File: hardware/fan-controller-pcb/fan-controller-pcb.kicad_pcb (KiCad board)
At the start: 2 copper layers, 91 x 121.5 mm, 42 parts, among them J1 Screw_Terminal_01x04, J2 nc3fdm3-v, J3 nc3mdm3-v, SW1 SW_SPDT, SW2 SW_DIP_x10, U1 MC7812BDTG, U2 MC7805CDTG, U3 MCP4922, U4 TLC272, U5 MAX485E

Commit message: update PCB: edge cuts, routing, symbol_lib, footprint_lib, art & data sheets
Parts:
- added kibuzzard-63FA74A1: G***, kibuzzard-63FA74A1, F.Cu at (90.3, 40.0)
- added kibuzzard-63FA74BB: G***, kibuzzard-63FA74BB, F.Cu at (85.3, 40.0)
- added kibuzzard-63FA74F3: G***, kibuzzard-63FA74F3, F.Cu at (75.3, 40.0)
- added kibuzzard-63FA7528: G***, kibuzzard-63FA7528, F.Cu at (80.3, 40.0)
- added kibuzzard-640DCC4D: G***, kibuzzard-640DCC4D, F.Cu at (156.6, 39.0)
- added kibuzzard-640DCC52: G***, kibuzzard-640DCC52, F.Cu at (155.0, 73.3)
- added kibuzzard-640DCC68: G***, kibuzzard-640DCC68, F.Cu at (111.3, 127.3)
- added kibuzzard-640DCC6D: G***, kibuzzard-640DCC6D, F.Cu at (149.2, 126.5)
- added kibuzzard-640DCC72: G***, kibuzzard-640DCC72, F.Cu at (151.2, 91.9)
- added kibuzzard-640DCC79: G***, kibuzzard-640DCC79, F.Cu at (77.0, 127.3)
- added kibuzzard-640DCC82: G***, kibuzzard-640DCC82, F.Cu at (112.9, 65.4)
- added kibuzzard-640DCCF2: G***, kibuzzard-640DCCF2, F.Cu at (249.8, 90.2)
- moved C5 214.0 mm to (138.2, 106.8), turned to 0 degrees
- moved U4 213.7 mm to (140.0, 102.8), turned to 180 degrees
- moved U3 197.3 mm to (140.0, 93.0)
- moved R15 194.7 mm to (152.4, 103.0), turned to 180 degrees
- moved R17 194.1 mm to (152.4, 105.0), turned to 0 degrees
- moved C6 189.1 mm to (146.2, 93.3), turned to 90 degrees
- moved SW2 69.1 mm to (156.0, 53.0)
- moved SW1 66.0 mm to (145.0, 119.0)
- moved C4 55.3 mm to (126.5, 57.5), turned to 90 degrees
- moved C2 54.9 mm to (126.5, 40.6), turned to 90 degrees
- moved U2 52.1 mm to (120.0, 57.0), turned to -90 degrees
- moved U1 51.4 mm to (120.0, 40.0), turned to -90 degrees
- moved C3 48.5 mm to (113.5, 57.5), turned to 90 degrees
- moved C1 46.9 mm to (113.5, 40.6), turned to 90 degrees
- moved R16 41.9 mm to (120.0, 68.0)
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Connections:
- A1 pad 19: DIP_8 -> DIP_10
- A1 pad 21: DIP_10 -> DIP_8
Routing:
- net +5V: track 0.00 -> 140.1 mm, vias 0 -> 4
- net Net-(J1-Pad3): track 0.00 -> 130.1 mm
- net +12V: track 0.00 -> 123.8 mm, vias 0 -> 1
- net +24V: track 0.00 -> 78.9 mm
- net DIP_8: track 0.00 -> 64.7 mm
- net DIP_10: track 0.00 -> 64.2 mm
- net DIP_9: track 0.00 -> 64.2 mm
- net DMX_D+: track 0.00 -> 64.1 mm
- net DMX_D-: track 0.00 -> 61.9 mm
- net Net-(D1-Pad2): track 0.00 -> 49.4 mm, vias 0 -> 1
- net 1.6V-10V_2: track 0.00 -> 47.2 mm
- net DIP_3: track 0.00 -> 44.1 mm
- net DIP_2: track 0.00 -> 43.9 mm
- net DIP_1: track 0.00 -> 43.7 mm
- net DIP_4: track 0.00 -> 43.2 mm
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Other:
- board size 91 x 121.5 mm -> 100 x 130 mm
- board text added: "DMX0"
- board text added: "DMX1"
- board text added: "DMX2"
- board text added: "DMX3"
- board text added: "DMX4"
- board text added: "DMX5"
- board text added: "DMX6"
- board text added: "DMX7"
- board text added: "DMX8"
- board text added: "FUNC"
- board text added: "GND"
- board text added: "LED+"
- board text added: "github.com/LennardBoediger/dmx-fan-controller"

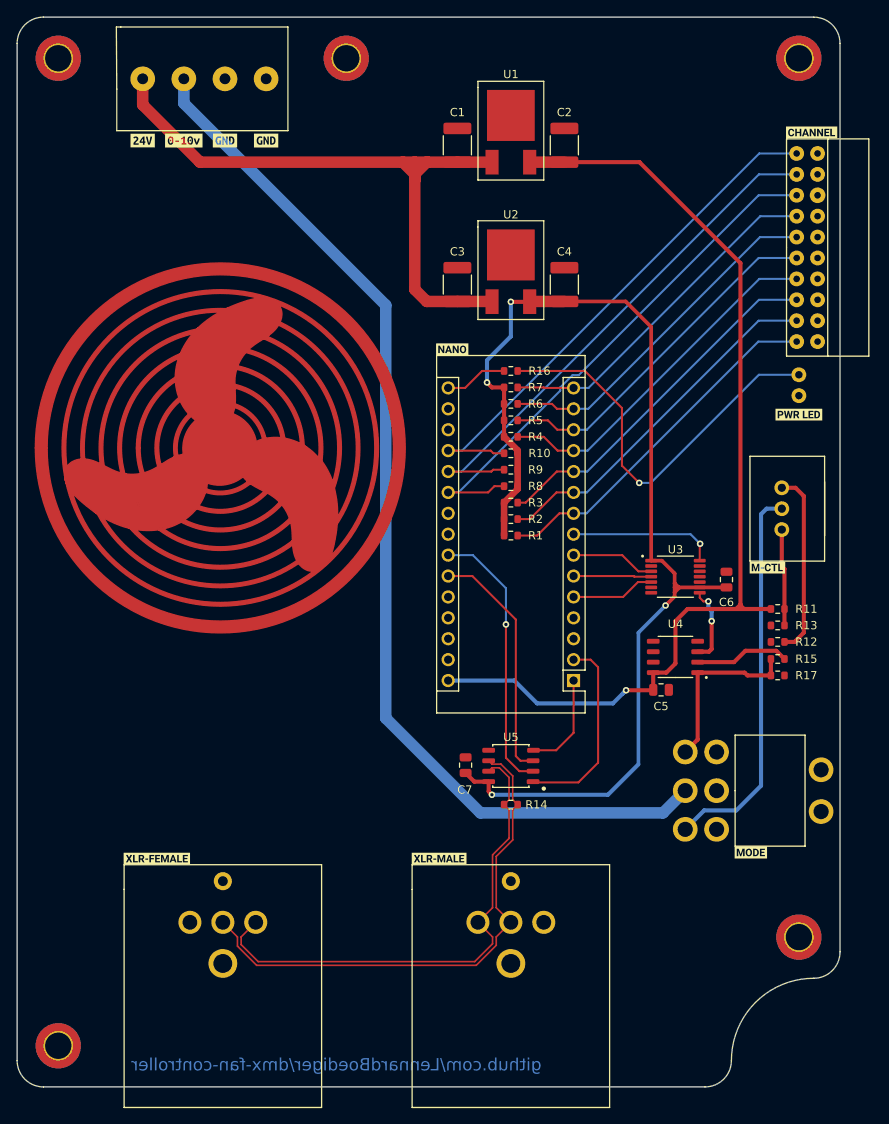
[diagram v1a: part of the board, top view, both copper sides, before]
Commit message: update PCB: add GND-plane & PCB Name
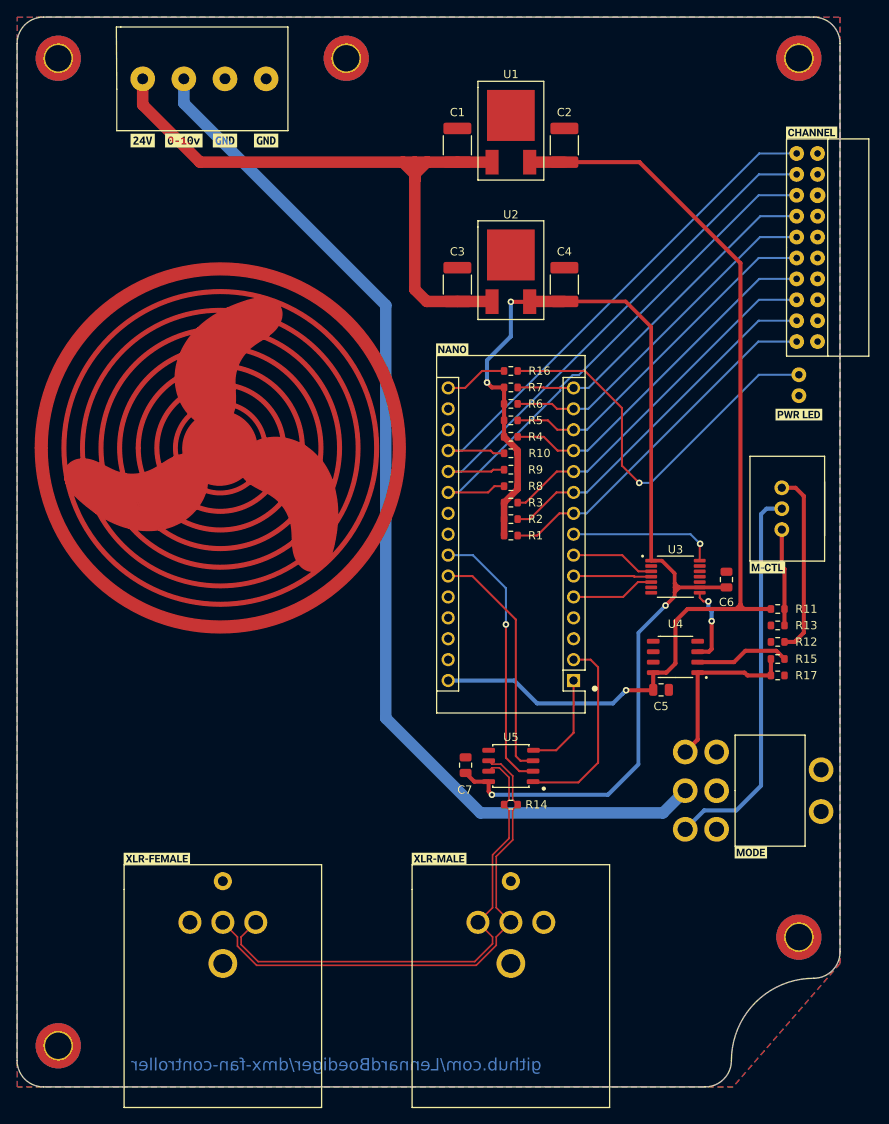
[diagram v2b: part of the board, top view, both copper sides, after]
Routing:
- added copper zone on B.Cu, net GND
- added copper zone on F.Cu, net GND
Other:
- board text added: "DMX FAN CONTROLLER Rev: v1"
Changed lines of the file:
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@@
       (xy 90.401195 63.789544)
     ) (layer "F.Cu") (width 0.17) (fill solid))
+  (gr_circle (center 130.2 106.6) (end 130.520156 106.6) (layer "F.SilkS") (width 0.1) (fill solid))
   (gr_poly
     (pts
@@
     (effects (font (size 1 1) (thickness 0.15)) (justify left mirror))
   )
+  (gr_text "DMX FAN CONTROLLER Rev: v1" (at 147.2 30) (layer "B.SilkS")
+    (effects (font (size 1.5 1.5) (thickness 0.3)) (justify left mirror))
+  )
   (gr_text "FUNC" (at 153.33 41.57) (layer "B.SilkS")
     (effects (font (size 1 1) (thickness 0.15)) (justify left mirror))
@@
   (segment (start 144.4 97.2) (end 144 96.8) (width 0.5) (layer "B.Cu") (net 39))
   (segment (start 144 96.8) (end 144 96) (width 0.5) (layer "B.Cu") (net 39))
+  (zone (net 3) (net_name "GND") (layers F&B.Cu) (hatch edge 0.508)
+    (connect_pads (clearance 0))
+    (min_thickness 0.254) (filled_areas_thickness no)
+    (fill yes (thermal_gap 0.508) (thermal_bridge_width 0.508))
+    (polygon
+      (pts
+        (xy 160 140)
+        (xy 147 155)
+        (xy 60 155)
+        (xy 60 25)
+        (xy 160 25)
+      )
+    )
+  )
   (zone (net 0) (net_name "") (layers "F.Cu" "F.Adhes" "F.Paste" "F.SilkS" "F.Mask") (hatch full 0.508)
     (connect_pads (clearance 0))

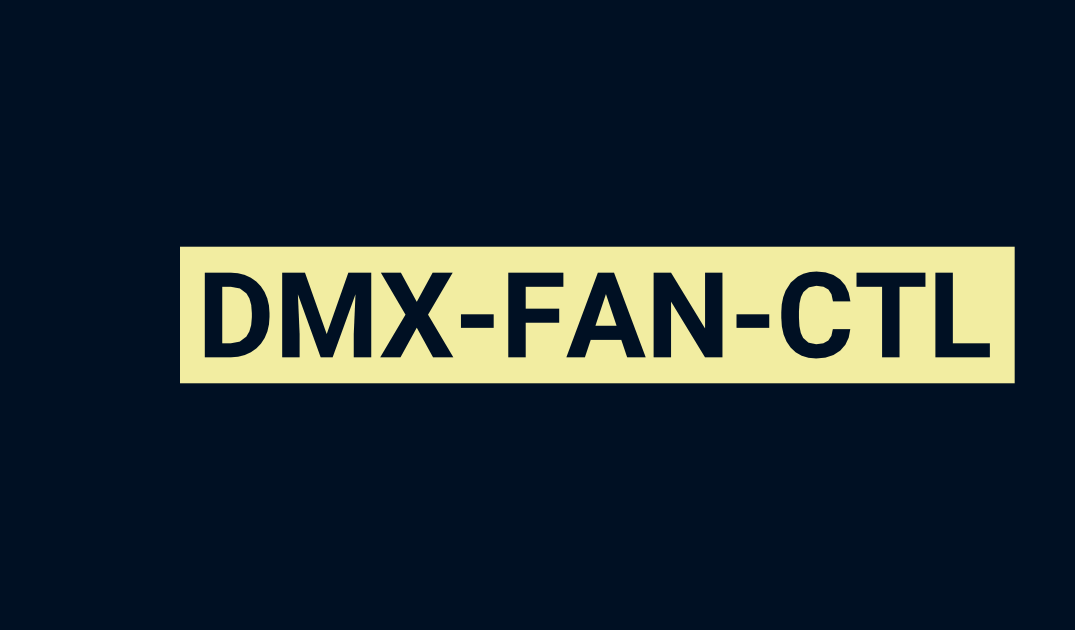
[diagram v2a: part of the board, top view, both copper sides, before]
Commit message: add Schematic as svg
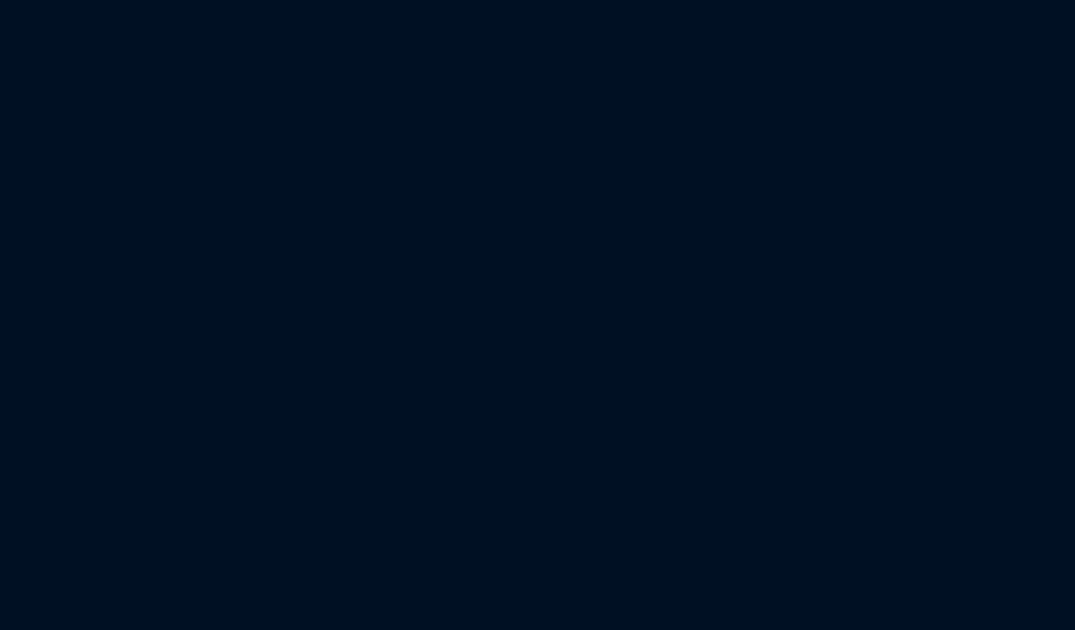
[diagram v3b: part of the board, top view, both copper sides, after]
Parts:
- removed kibuzzard-640DCCF2: G***, kibuzzard-640DCCF2
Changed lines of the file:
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@@
     )
-  )
-  (footprint "kibuzzard-640DCCF2" (layer "F.Cu")
-    (at 249.75 90.15)
-    (descr "Generated with KiBuzzard")
-    (tags "kb_params=eyJBbGlnbm1lbnRDaG9pY2UiOiAiTGVmdCIsICJDYXBMZWZ0Q2hvaWNlIjogIlsiLCAiQ2FwUmlnaHRDaG9pY2UiOiAiXSIsICJGb250Q29tYm9Cb3giOiAiUm9ib3RvLUJvbGQiLCAiSGVpZ2h0Q3RybCI6ICIyLjUiLCAiTGF5ZXJDb21ib0JveCI6ICJGLlNpbGtTIiwgIk11bHRpTGluZVRleHQiOiAiRE1YLUZBTi1DVEwiLCAiUGFkZGluZ0JvdHRvbUN0cmwiOiAiNSIsICJQYWRkaW5nTGVmdEN0cmwiOiAiNSIsICJQYWRkaW5nUmlnaHRDdHJsIjogIjUiLCAiUGFkZGluZ1RvcEN0cmwiOiAiNSIsICJXaWR0aEN0cmwiOiAiMyJ9")
-    (attr board_only exclude_from_pos_files exclude_from_bom)
-    (fp_text reference "kibuzzard-640DCCF2" (at 0 -5.324347) (layer "F.SilkS") hide
-      (effects (font (size 0 0) (thickness 0.15)))
-    )
-    (fp_text value "G***" (at 0 5.324347) (layer "F.SilkS") hide
-      (effects (font (size 0 0) (thickness 0.15)))
-    )
-    (fp_poly (pts
-        (xy -13.084473 -2.276347)
-        (xy -13.911296 -2.276347)
-        (xy -13.911296 2.276347)
-        (xy -13.084473 2.276347)
-        (xy -13.084473 1.410767)
-        (xy -13.084473 -1.410767)
-        (xy -12.216309 -1.410767)
-        (xy -11.976982 -1.392142)
-        (xy -11.755096 -1.336266)
-        (xy -11.550652 -1.243141)
-        (xy -11.369246 -1.115673)
-        (xy -11.216477 -0.956768)
-        (xy -11.092346 -0.766426)
-        (xy -11.000836 -0.551)
-        (xy -10.94593 -0.316841)
-        (xy -10.927628 -0.06395)
-        (xy -10.927628 0.065887)
-        (xy -10.945607 0.318456)
-        (xy -10.999544 0.551646)
-        (xy -11.089439 0.765457)
-        (xy -11.212063 0.954291)
-        (xy -11.364186 1.112551)
-        (xy -11.545807 1.240234)
-        (xy -11.750575 1.334113)
-        (xy -11.972137 1.390957)
-        (xy -12.210495 1.410767)
-        (xy -13.084473 1.410767)
-        (xy -13.084473 2.276347)
-        (xy -7.536362 2.276347)
-        (xy -7.536362 1.410767)
-        (xy -8.119659 1.410767)
-        (xy -8.119659 0.639496)
-        (xy -8.061523 -0.691818)
-        (xy -8.823105 1.410767)
-        (xy -9.222305 1.410767)
-        (xy -9.981949 -0.68988)
-        (xy -9.923813 0.639496)
-        (xy -9.923813 1.410767)
-        (xy -10.505173 1.410767)
-        (xy -10.505173 -1.410767)
-        (xy -9.745529 -1.410767)
-        (xy -9.020767 0.63562)
-        (xy -8.299881 -1.410767)
-        (xy -7.536362 -1.410767)
-        (xy -7.536362 1.410767)
-        (xy -7.536362 2.276347)
-        (xy -4.800095 2.276347)
-        (xy -4.800095 1.410767)
-        (xy -5.47641 1.410767)
-        (xy -6.019012 0.422455)
-        (xy -6.561615 1.410767)
-        (xy -7.23793 1.410767)
-        (xy -6.394958 -0.011627)
-        (xy -7.216614 -1.410767)
-        (xy -6.54805 -1.410767)
-        (xy -6.019012 -0.437958)
-        (xy -5.489975 -1.410767)
-        (xy -4.821411 -1.410767)
-        (xy -5.643066 -0.011627)
-        (xy -4.800095 1.410767)
-        (xy -4.800095 2.276347)
-        (xy -3.455215 2.276347)
-        (xy -3.455215 0.428268)
-        (xy -4.546234 0.428268)
-        (xy -4.546234 -0.023254)
-        (xy -3.455215 -0.023254)
-        (xy -3.455215 0.428268)
-        (xy -3.455215 2.276347)
-        (xy -2.387451 2.276347)
-        (xy -2.387451 1.410767)
-        (xy -2.968811 1.410767)
-        (xy -2.968811 -1.410767)
-        (xy -1.131714 -1.410767)
-        (xy -1.131714 -0.939865)
-        (xy -2.387451 -0.939865)
-        (xy -2.387451 -0.211227)
-        (xy -1.27124 -0.211227)
-        (xy -1.27124 0.257736)
-        (xy -2.387451 0.257736)
-        (xy -2.387451 1.410767)
-        (xy -2.387451 2.276347)
-        (xy -0.414703 2.276347)
-        (xy -0.414703 1.410767)
-        (xy -1.032883 1.410767)
-        (xy 0.017441 -1.410767)
-        (xy 0.556168 -1.410767)
-        (xy 1.612305 1.410767)
-        (xy 0.994125 1.410767)
-        (xy 0.798401 0.829407)
-        (xy -0.220917 0.829407)
-        (xy -0.414703 1.410767)
-        (xy -0.414703 2.276347)
-        (xy 4.170288 2.276347)
-        (xy 4.170288 1.410767)
-        (xy 3.588928 1.410767)
-        (xy 2.457214 -0.445709)
-        (xy 2.457214 1.410767)
-        (xy 1.875854 1.410767)
-        (xy 1.875854 -1.410767)
-        (xy 2.457214 -1.410767)
-        (xy 3.590866 0.449585)
-        (xy 3.590866 -1.410767)
-        (xy 4.170288 -1.410767)
-        (xy 4.170288 1.410767)
-        (xy 4.170288 2.276347)
-        (xy 5.73027 2.276347)
-        (xy 5.73027 0.428268)
-        (xy 4.639252 0.428268)
-        (xy 4.639252 -0.023254)
-        (xy 5.73027 -0.023254)
-        (xy 5.73027 0.428268)
-        (xy 5.73027 2.276347)
-        (xy 7.296066 2.276347)
-        (xy 7.296066 1.449524)
-        (xy 7.039238 1.426693)
-        (xy 6.811357 1.358202)
-        (xy 6.612423 1.24405)
-        (xy 6.442436 1.084236)
-        (xy 6.306362 0.884575)
-        (xy 6.209166 0.650881)
-        (xy 6.150848 0.383152)
-        (xy 6.131409 0.08139)
-        (xy 6.131409 -0.09108)
-        (xy 6.147342 -0.351615)
-        (xy 6.195143 -0.590619)
-        (xy 6.274811 -0.80809)
-        (xy 6.448977 -1.082056)
-        (xy 6.684669 -1.283836)
-        (xy 6.871889 -1.375885)
-        (xy 7.078272 -1.431114)
-        (xy 7.303818 -1.449524)
-        (xy 7.608278 -1.420456)
-        (xy 7.870536 -1.333252)
-        (xy 8.090591 -1.187912)
-        (xy 8.261554 -0.990034)
-        (xy 8.376534 -0.745217)
-        (xy 8.435532 -0.453461)
-        (xy 7.854172 -0.453461)
-        (xy 7.805483 -0.689154)
-        (xy 7.702049 -0.849754)
-        (xy 7.537088 -0.942045)
-        (xy 7.303818 -0.972809)
-        (xy 7.049715 -0.920729)
-        (xy 6.868767 -0.764488)
-        (xy 6.78813 -0.600093)
-        (xy 6.738714 -0.384666)
-        (xy 6.72052 -0.11821)
-        (xy 6.72052 0.094955)
-        (xy 6.735915 0.372501)
-        (xy 6.782101 0.595356)
-        (xy 6.859077 0.763519)
-        (xy 7.037603 0.92194)
-        (xy 7.296066 0.974747)
-        (xy 7.531275 0.943983)
-        (xy 7.698174 0.851692)
-        (xy 7.802576 0.694967)
-        (xy 7.850296 0.470901)
-        (xy 8.431656 0.470901)
-        (xy 8.379656 0.752969)
-        (xy 8.267583 0.991972)
-        (xy 8.095436 1.187912)
-        (xy 7.871828 1.333252)
-        (xy 7.605371 1.420456)
-        (xy 7.296066 1.449524)
-        (xy 7.296066 2.276347)
-        (xy 10.073029 2.276347)
-        (xy 10.073029 1.410767)
-        (xy 9.491669 1.410767)
-        (xy 9.491669 -0.939865)
-        (xy 8.639008 -0.939865)
-        (xy 8.639008 -1.410767)
-        (xy 10.937317 -1.410767)
-        (xy 10.937317 -0.939865)
-        (xy 10.073029 -0.939865)
-        (xy 10.073029 1.410767)
-        (xy 10.073029 2.276347)
-        (xy 13.084473 2.276347)
-        (xy 13.084473 1.410767)
-        (xy 11.268692 1.410767)
-        (xy 11.268692 -1.410767)
-        (xy 11.850052 -1.410767)
-        (xy 11.850052 0.943741)
-        (xy 13.084473 0.943741)
-        (xy 13.084473 1.410767)
-        (xy 13.084473 2.276347)
-        (xy 13.911296 2.276347)
-        (xy 13.911296 -2.276347)
-        (xy 13.084473 -2.276347)
-        (xy -13.084473 -2.276347)
-      ) (layer "F.SilkS") (width 0) (fill solid))
-    (fp_poly (pts
-        (xy -12.503113 -0.939865)
-        (xy -12.503113 0.943741)
-        (xy -12.222122 0.943741)
-        (xy -11.921268 0.888027)
-        (xy -11.700836 0.720886)
-        (xy -11.600282 0.551)
-        (xy -11.538917 0.338481)
-        (xy -11.516739 0.083328)
-        (xy -11.516739 -0.065887)
-        (xy -11.536548 -0.329545)
-        (xy -11.595976 -0.546909)
-        (xy -11.695023 -0.717979)
-        (xy -11.914486 -0.884394)
-        (xy -12.216309 -0.939865)
-        (xy -12.503113 -0.939865)
-      ) (layer "F.SilkS") (width 0) (fill solid))
-    (fp_poly (pts
-        (xy -0.06395 0.358505)
-        (xy 0.641434 0.358505)
-        (xy 0.286804 -0.697632)
-        (xy -0.06395 0.358505)
-      ) (layer "F.SilkS") (width 0) (fill solid))
   )
   (footprint "Resistor_SMD:R_0603_1608Metric" (layer "F.Cu")
